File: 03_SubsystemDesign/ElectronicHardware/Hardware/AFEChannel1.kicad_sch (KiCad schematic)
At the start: 30 parts, among them U2001 OPA690xDBV, U2002 AD8139

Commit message: pcb design work in progress
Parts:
- removed C2002, C2005, C2007, C2011: C, Capacitor_SMD:C_0805_2012Metric, symbol Device:C
- removed U2001: OPA690xDBV, Package_TO_SOT_SMD:SOT-23-6, symbol Amplifier_Operational:OPA690xDBV
- added C408, C409: C, Capacitor_SMD:C_0805_2012Metric, symbol Device:C
- added D401: D_SiPM, symbol Device:D_SiPM
- added U403: LTC6268xS6-10, Package_TO_SOT_SMD:TSOT-23-6, symbol Amplifier_Operational:LTC6268xS6-10
- C2003: value C -> 2n2
- C2012: value C -> 150p
- C2013, C2016, C2017: value C -> 100p
- R2001: value R -> 2k
- RN2001: value R_Pack04 -> 1k
- RN2002: value R_Pack04 -> 620R
- RN2003, RN2004: value R_Pack04 -> 100R
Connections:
- net -3V3_A is gone; now on net GND: U2002.6 (V-)
- net 1V5_REF: now also C408.1, C409.1, U403.3 (+)
- net GND: now also C408.2, C409.2, U403.2 (V-)
- net SIPM_BIAS: now also D401.1 (K)
- net at C2003.2, R2001.1, RN2001.1 (R1.1)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: now also U403.1
- net at C2003.1, D2001.2 (A), R2001.2: now also D401.2 (A), U403.4 (-)
- net +3V3_A renamed +5V0_A
- net +5V0_A: now also U403.5 (~{SHDN}), U403.6 (V+)
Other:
- note added: "Anti-Aliasing Filter (AAF)"
- note removed: "10-20 MHz Anti-Aliasing Filter (AAF) Value TBD"
- note removed: "75MHz protects stability of diff opamp from ADC's switched-cap input kickback TBD check if needed?"
- moved on the sheet: C2001, C2003, C2004, C2006, C2008, C2009, C2010, C2012, C2013, C2014, C2015, C2016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

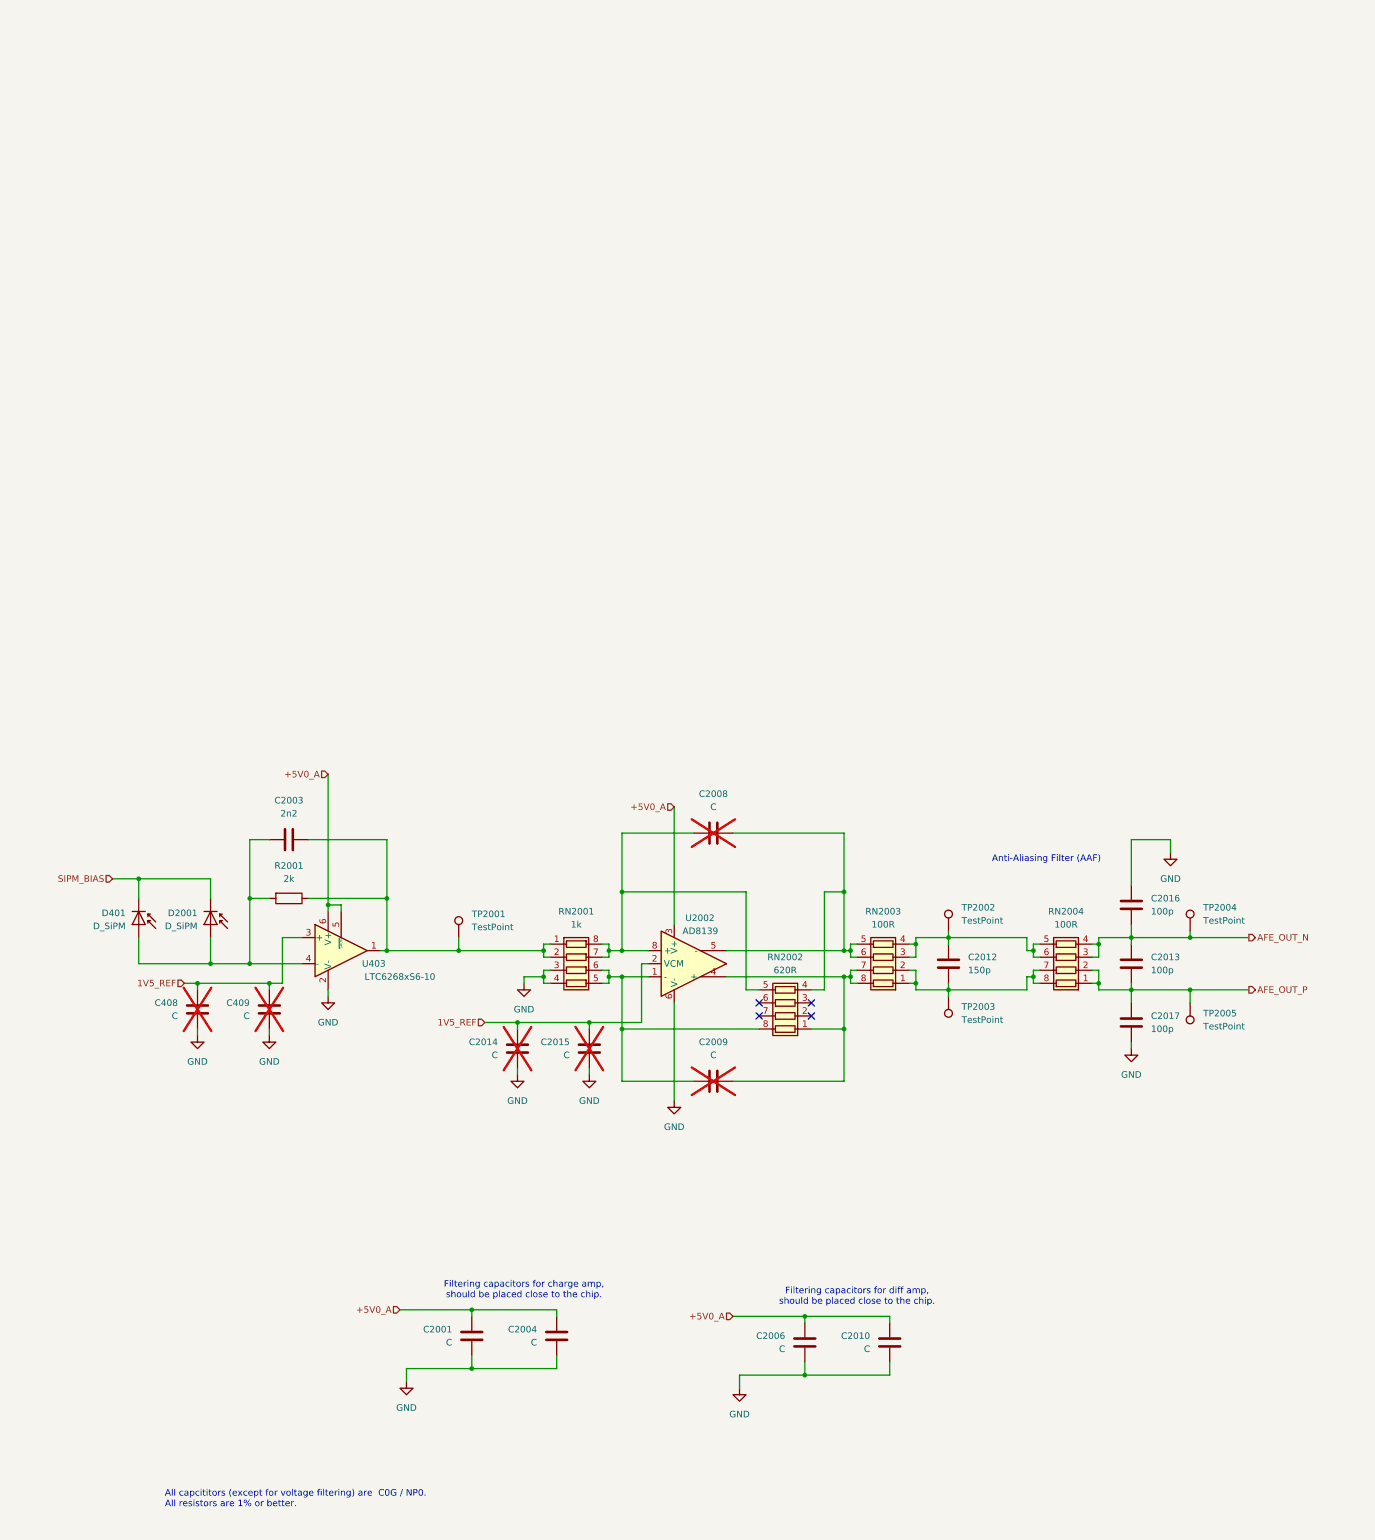
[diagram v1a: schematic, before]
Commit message: improve CAD folder structure and PCB
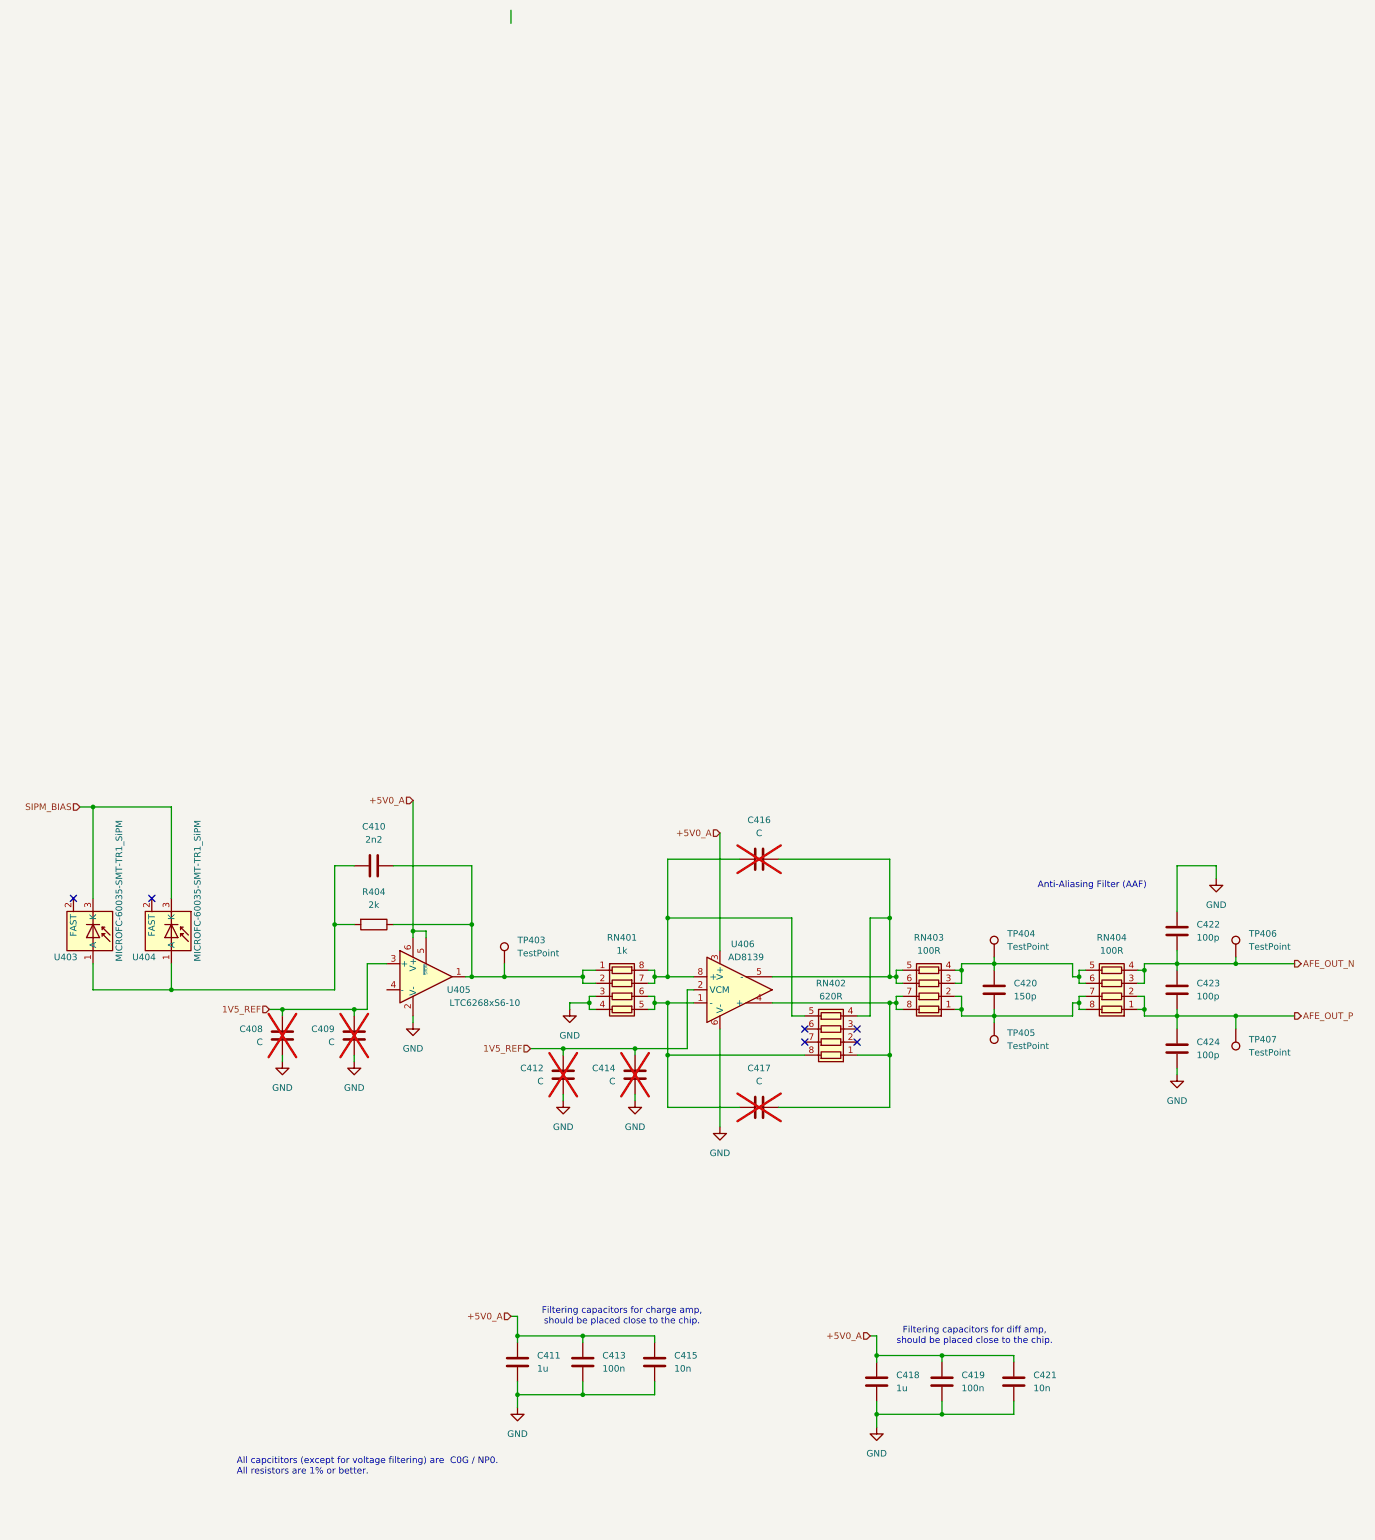
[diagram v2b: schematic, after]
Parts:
- removed C2001, C2004, C2006, C2008, C2009, C2010, C2014, C2015: C, Capacitor_SMD:C_0805_2012Metric, symbol Device:C
- removed C2003: 2n2, Capacitor_SMD:C_0805_2012Metric, symbol Device:C
- removed C2012: 150p, Capacitor_SMD:C_0805_2012Metric, symbol Device:C
- removed C2013, C2016, C2017: 100p, Capacitor_SMD:C_0805_2012Metric, symbol Device:C
- removed D2001, D401: D_SiPM, symbol Device:D_SiPM
- removed R2001: 2k, Resistor_SMD:R_0805_2012Metric, symbol Device:R
- removed RN2001: 1k, Resistor_SMD:R_Array_Convex_4x0612, symbol Device:R_Pack04
- removed RN2002: 620R, Resistor_SMD:R_Array_Convex_4x0612, symbol Device:R_Pack04
- removed RN2003, RN2004: 100R, Resistor_SMD:R_Array_Convex_4x0612, symbol Device:R_Pack04
- removed TP2001, TP2002, TP2003, TP2004, TP2005: TestPoint, TestPoint:TestPoint_Pad_D1.0mm, symbol Connector:TestPoint
- removed U2002: AD8139, Package_SO:SOIC-8_5.3x5.3mm_P1.27mm, symbol GammaSpectrometer:AD8139
- removed U403: LTC6268xS6-10, Package_TO_SOT_SMD:TSOT-23-6, symbol Amplifier_Operational:LTC6268xS6-10
- added C410: 2n2, Capacitor_SMD:C_0805_2012Metric, symbol Device:C
- added C411, C418: 1u, Capacitor_SMD:C_0805_2012Metric, symbol Device:C
- added C412, C414, C416, C417: C, Capacitor_SMD:C_0805_2012Metric, symbol Device:C
- added C413, C419: 100n, Capacitor_SMD:C_0805_2012Metric, symbol Device:C
- added C415, C421: 10n, Capacitor_SMD:C_0805_2012Metric, symbol Device:C
- added C420: 150p, Capacitor_SMD:C_0805_2012Metric, symbol Device:C
- added C422, C423, C424: 100p, Capacitor_SMD:C_0805_2012Metric, symbol Device:C
- added R404: 2k, Resistor_SMD:R_0805_2012Metric, symbol Device:R
- added RN401: 1k, Resistor_SMD:R_Array_Convex_4x0612, symbol Device:R_Pack04
- added RN402: 620R, Resistor_SMD:R_Array_Convex_4x0612, symbol Device:R_Pack04
- added RN403, RN404: 100R, Resistor_SMD:R_Array_Convex_4x0612, symbol Device:R_Pack04
- added TP403, TP404, TP405, TP406, TP407: TestPoint, TestPoint:TestPoint_Pad_D1.0mm, symbol Connector:TestPoint
- added U403, U404: MICROFC-60035-SMT-TR1_SiPM, GammaSpectrometer:MICROFC-60035-SMT-TR1_SiPM, symbol GammaSpectrometer:MICROFC-60035-SMT-TR1_SiPM
- added U405: LTC6268xS6-10, Package_TO_SOT_SMD:TSOT-23-6, symbol Amplifier_Operational:LTC6268xS6-10
- added U406: AD8139, Package_SO:SOIC-8_5.3x5.3mm_P1.27mm, symbol GammaSpectrometer:AD8139
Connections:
- net +5V0_A: now also C411.1, C413.1, C415.1, C418.1, C419.1, C421.1, U405.5 (~{SHDN}), U405.6 (V+), U406.3 (V+)
- net 1V5_REF: now also C412.1, C414.1, U405.3 (+), U406.2 (VCM)
- net AFE_OUT_N: now also C422.1, C423.2, RN404.3 (R3.1), RN404.4 (R4.1), TP406.1
- net AFE_OUT_P: now also C423.1, C424.2, RN404.1 (R1.1), RN404.2 (R2.1), TP407.1
- net GND: now also C411.2, C412.2, C413.2, C414.2, C415.2, C418.2, C419.2, C421.2, C422.2, C424.1, RN401.3 (R3.1), RN401.4 (R4.1), U405.2 (V-), U406.6 (V-)
- net SIPM_BIAS: now also U403.3 (K), U404.3 (K)
- new net: C410.2, R404.1, RN401.1 (R1.1), RN401.2 (R2.1), TP403.1, U405.1
- new net: C410.1, R404.2, U403.1 (A), U404.1 (A)
- new net: C417.1, RN401.5 (R4.2), RN401.6 (R3.2), RN402.8 (R1.2), U406.1 (-)
- new net: C416.1, RN401.7 (R2.2), RN401.8 (R1.2), RN402.5 (R4.2), U406.8 (+)
- new net: C416.2, RN402.4 (R4.1), RN403.5 (R4.2), RN403.6 (R3.2), U406.5 (-)
- new net: C417.2, RN402.1 (R1.1), RN403.7 (R2.2), RN403.8 (R1.2), U406.4 (+)
- new net: C420.1, RN403.1 (R1.1), RN403.2 (R2.1), RN404.7 (R2.2), RN404.8 (R1.2), TP405.1
- new net: C420.2, RN403.3 (R3.1), RN403.4 (R4.1), RN404.5 (R4.2), RN404.6 (R3.2), TP404.1
- no-connect marks 4 -> 6
